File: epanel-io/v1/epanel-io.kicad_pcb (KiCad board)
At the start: 2 copper layers, 87 x 68 mm, 38 parts, among them J1 Conn_01x05_Male, J2 Screw_Terminal_01x03, J3 Screw_Terminal_01x03, Q1 IRF830, Q2 IRF830, Q3 IRF830, Q4 IRF830, U1 Pico, U2 4N35, U3 4N35, U4 H11AA1, U5 H11AA1, U6 H11AA1

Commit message: ok let's go!
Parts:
- removed JP1: Jumper_2_Bridged, Connector_PinHeader_2.54mm:PinHeader_1x02_P2.54mm_Vertical
- removed PS1: HLK-PM01, Converter_ACDC:Converter_ACDC_HiLink_HLK-PMxx
- added C10: 2.2uF/63V, Capacitor_SMD:C_1206_3216Metric, F.Cu at (434.5, 170.8)
- added C3: 2.2uF/63V, Capacitor_SMD:C_1206_3216Metric, F.Cu at (435.5, 59.6)
- added C4: 2.2uF/63V, Capacitor_SMD:C_1206_3216Metric, F.Cu at (356.4, 181.3)
- added C5: 2.2uF/63V, Capacitor_SMD:C_1206_3216Metric, F.Cu at (538.9, 59.6)
- added C6: 2.2uF/63V, Capacitor_SMD:C_1206_3216Metric, F.Cu at (472.8, 59.6)
- added C7: 2.2uF/63V, Capacitor_SMD:C_1206_3216Metric, F.Cu at (493.2, 115.2)
- added C8: 2.2uF/63V, Capacitor_SMD:C_1206_3216Metric, F.Cu at (509.1, 170.8)
- added C9: 2.2uF/63V, Capacitor_SMD:C_1206_3216Metric, F.Cu at (576.2, 59.6)
- added D10: 1N4007, Diode_SMD:D_SMA, F.Cu at (540.1, 55.6)
- added D11: 10V/0.4W, Diode_SMD:D_SOD-123, F.Cu at (490.5, 39.6)
- added D12: 1N4007, Diode_SMD:D_SMA, F.Cu at (474.0, 55.6)
- added D13: 10V/0.4W, Diode_SMD:D_SOD-123, F.Cu at (510.9, 95.2)
- added D14: 1N4007, Diode_SMD:D_SMA, F.Cu at (494.4, 111.3)
- added D15: 10V/0.4W, Diode_SMD:D_SOD-123, F.Cu at (526.8, 150.8)
- added D16: 1N4007, Diode_SMD:D_SMA, F.Cu at (510.3, 166.9)
- added D17: 10V/0.4W, Diode_SMD:D_SOD-123, F.Cu at (594.0, 39.6)
- added D18: 1N4007, Diode_SMD:D_SMA, F.Cu at (577.4, 55.6)
- added D19: 10V/0.4W, Diode_SMD:D_SOD-123, F.Cu at (452.2, 150.8)
- added D20: 1N4007, Diode_SMD:D_SMA, F.Cu at (435.7, 166.9)
- added D5: 10V/0.4W, Diode_SMD:D_SOD-123, F.Cu at (453.2, 39.6)
- added D6: 1N4007, Diode_SMD:D_SMA, F.Cu at (436.7, 55.6)
- added D7: 10V/0.4W, Diode_SMD:D_SOD-123, F.Cu at (374.1, 161.3)
- added D8: 1N4007, Diode_SMD:D_SMA, F.Cu at (357.6, 177.4)
- added D9: 10V/0.4W, Diode_SMD:D_SOD-123, F.Cu at (556.7, 39.6)
- added J4: Screw_Terminal_01x05, TerminalBlock:TerminalBlock_bornier-5_P5.08mm, F.Cu at (319.5, 86.8)
- added J5: Screw_Terminal_01x05, TerminalBlock:TerminalBlock_bornier-5_P5.08mm, F.Cu at (343.6, 42.2)
- added J6: Screw_Terminal_01x03, TerminalBlock:TerminalBlock_bornier-3_P5.08mm, F.Cu at (343.6, 51.3)
- added J7: Screw_Terminal_01x03, TerminalBlock:TerminalBlock_bornier-3_P5.08mm, F.Cu at (370.5, 42.2)
- added Q10: IRF830, Package_TO_SOT_SMD:TO-263-3_TabPin2, F.Cu at (544.9, 47.2)
- added Q11: IRF830, Package_TO_SOT_SMD:TO-263-3_TabPin2, F.Cu at (478.8, 34.8)
- added Q12: IRF830, Package_TO_SOT_SMD:TO-263-3_TabPin2, F.Cu at (478.8, 47.2)
- added Q13: IRF830, Package_TO_SOT_SMD:TO-263-3_TabPin2, F.Cu at (499.2, 90.5)
- added Q14: IRF830, Package_TO_SOT_SMD:TO-263-3_TabPin2, F.Cu at (499.2, 102.8)
- added Q15: IRF830, Package_TO_SOT_SMD:TO-263-3_TabPin2, F.Cu at (515.1, 146.1)
- added Q16: IRF830, Package_TO_SOT_SMD:TO-263-3_TabPin2, F.Cu at (515.1, 158.4)
- added Q17: IRF830, Package_TO_SOT_SMD:TO-263-3_TabPin2, F.Cu at (582.2, 34.8)
- added Q18: IRF830, Package_TO_SOT_SMD:TO-263-3_TabPin2, F.Cu at (582.2, 47.2)
- added Q19: IRF830, Package_TO_SOT_SMD:TO-263-3_TabPin2, F.Cu at (440.5, 146.1)
- added Q20: IRF830, Package_TO_SOT_SMD:TO-263-3_TabPin2, F.Cu at (440.5, 158.4)
- added Q5: IRF830, Package_TO_SOT_SMD:TO-263-3_TabPin2, F.Cu at (441.5, 34.8)
- added Q6: IRF830, Package_TO_SOT_SMD:TO-263-3_TabPin2, F.Cu at (441.5, 47.2)
- added Q7: IRF830, Package_TO_SOT_SMD:TO-263-3_TabPin2, F.Cu at (362.4, 156.6)
- added Q8: IRF830, Package_TO_SOT_SMD:TO-263-3_TabPin2, F.Cu at (362.4, 168.9)
- added Q9: IRF830, Package_TO_SOT_SMD:TO-263-3_TabPin2, F.Cu at (544.9, 34.8)
- added R18: 10KΩ, Resistor_SMD:R_0603_1608Metric, F.Cu at (404.8, 153.3)
- added R19: 33KΩ/0.5W, Resistor_SMD:R_0805_2012Metric, F.Cu at (418.2, 141.4)
- added R20: 33KΩ/0.5W, Resistor_SMD:R_0805_2012Metric, F.Cu at (405.0, 150.6)
- added R21: 330Ω, Resistor_SMD:R_0603_1608Metric, F.Cu at (434.6, 62.5)
- added R22: 22KΩ, Resistor_SMD:R_0603_1608Metric, F.Cu at (463.6, 32.9)
- added R23: 33KΩ/0.5W, Resistor_SMD:R_0805_2012Metric, F.Cu at (442.9, 54.8)
- added R24: 33KΩ/0.5W, Resistor_SMD:R_0805_2012Metric, F.Cu at (463.8, 30.1)
- added R25: 10KΩ, Resistor_SMD:R_0603_1608Metric, F.Cu at (463.5, 97.7)
- added R26: 33KΩ/0.5W, Resistor_SMD:R_0805_2012Metric, F.Cu at (476.8, 85.8)
- added R27: 33KΩ/0.5W, Resistor_SMD:R_0805_2012Metric, F.Cu at (463.7, 95.0)
- added R28: 330Ω, Resistor_SMD:R_0603_1608Metric, F.Cu at (355.6, 184.3)
- added R29: 22KΩ, Resistor_SMD:R_0603_1608Metric, F.Cu at (384.5, 154.6)
- added R30: 33KΩ/0.5W, Resistor_SMD:R_0805_2012Metric, F.Cu at (363.8, 176.6)
- added R31: 33KΩ/0.5W, Resistor_SMD:R_0805_2012Metric, F.Cu at (384.7, 151.9)
- added R32: 10KΩ, Resistor_SMD:R_0603_1608Metric, F.Cu at (318.3, 108.3)
- added R33: 33KΩ/0.5W, Resistor_SMD:R_0805_2012Metric, F.Cu at (331.6, 96.3)
- added R34: 33KΩ/0.5W, Resistor_SMD:R_0805_2012Metric, F.Cu at (318.5, 105.5)
- added R35: 330Ω, Resistor_SMD:R_0603_1608Metric, F.Cu at (538.1, 62.5)
- added R36: 22KΩ, Resistor_SMD:R_0603_1608Metric, F.Cu at (567.0, 32.9)
- added R37: 33KΩ/0.5W, Resistor_SMD:R_0805_2012Metric, F.Cu at (546.3, 54.8)
- added R38: 33KΩ/0.5W, Resistor_SMD:R_0805_2012Metric, F.Cu at (567.2, 30.1)
- added R39: 10KΩ, Resistor_SMD:R_0603_1608Metric, F.Cu at (509.2, 42.1)
- added R40: 33KΩ/0.5W, Resistor_SMD:R_0805_2012Metric, F.Cu at (522.6, 30.1)
- added R41: 33KΩ/0.5W, Resistor_SMD:R_0805_2012Metric, F.Cu at (509.4, 39.4)
- added R42: 330Ω, Resistor_SMD:R_0603_1608Metric, F.Cu at (471.9, 62.5)
- added R43: 22KΩ, Resistor_SMD:R_0603_1608Metric, F.Cu at (500.9, 32.9)
- added R44: 33KΩ/0.5W, Resistor_SMD:R_0805_2012Metric, F.Cu at (480.2, 54.8)
- added R45: 33KΩ/0.5W, Resistor_SMD:R_0805_2012Metric, F.Cu at (501.1, 30.1)
- added R46: 10KΩ, Resistor_SMD:R_0603_1608Metric, F.Cu at (405.8, 42.1)
- added R47: 33KΩ/0.5W, Resistor_SMD:R_0805_2012Metric, F.Cu at (419.1, 30.1)
- added R48: 33KΩ/0.5W, Resistor_SMD:R_0805_2012Metric, F.Cu at (406.0, 39.4)
- added R49: 330Ω, Resistor_SMD:R_0603_1608Metric, F.Cu at (492.3, 118.1)
- added R50: 22KΩ, Resistor_SMD:R_0603_1608Metric, F.Cu at (521.3, 88.5)
- added R51: 33KΩ/0.5W, Resistor_SMD:R_0805_2012Metric, F.Cu at (500.6, 110.5)
- added R52: 33KΩ/0.5W, Resistor_SMD:R_0805_2012Metric, F.Cu at (521.5, 85.8)
- added R53: 10KΩ, Resistor_SMD:R_0603_1608Metric, F.Cu at (405.8, 97.7)
- added R54: 33KΩ/0.5W, Resistor_SMD:R_0805_2012Metric, F.Cu at (419.1, 85.8)
- added R55: 33KΩ/0.5W, Resistor_SMD:R_0805_2012Metric, F.Cu at (406.0, 95.0)
- added R56: 330Ω, Resistor_SMD:R_0603_1608Metric, F.Cu at (508.3, 173.7)
- added R57: 22KΩ, Resistor_SMD:R_0603_1608Metric, F.Cu at (537.2, 144.1)
- added R58: 33KΩ/0.5W, Resistor_SMD:R_0805_2012Metric, F.Cu at (516.5, 166.1)
- added R59: 33KΩ/0.5W, Resistor_SMD:R_0805_2012Metric, F.Cu at (537.4, 141.4)
- added R60: 10KΩ, Resistor_SMD:R_0603_1608Metric, F.Cu at (434.6, 97.7)
- added R61: 33KΩ/0.5W, Resistor_SMD:R_0805_2012Metric, F.Cu at (448.0, 85.8)
- added R62: 33KΩ/0.5W, Resistor_SMD:R_0805_2012Metric, F.Cu at (434.8, 95.0)
- added R63: 330Ω, Resistor_SMD:R_0603_1608Metric, F.Cu at (575.4, 62.5)
- added R64: 22KΩ, Resistor_SMD:R_0603_1608Metric, F.Cu at (604.3, 32.9)
- added R65: 33KΩ/0.5W, Resistor_SMD:R_0805_2012Metric, F.Cu at (583.6, 54.8)
- added R66: 33KΩ/0.5W, Resistor_SMD:R_0805_2012Metric, F.Cu at (604.5, 30.1)
- added R67: 10KΩ, Resistor_SMD:R_0603_1608Metric, F.Cu at (529.6, 97.7)
- added R68: 33KΩ/0.5W, Resistor_SMD:R_0805_2012Metric, F.Cu at (543.0, 85.8)
- added R69: 33KΩ/0.5W, Resistor_SMD:R_0805_2012Metric, F.Cu at (529.8, 95.0)
- added R70: 330Ω, Resistor_SMD:R_0603_1608Metric, F.Cu at (433.7, 173.7)
- added R71: 22KΩ, Resistor_SMD:R_0603_1608Metric, F.Cu at (462.6, 144.1)
- added R72: 33KΩ/0.5W, Resistor_SMD:R_0805_2012Metric, F.Cu at (441.9, 166.1)
- added R73: 33KΩ/0.5W, Resistor_SMD:R_0805_2012Metric, F.Cu at (462.8, 141.4)
- added U10: 4N35, Package_DIP:SMDIP-6_W7.62mm, F.Cu at (376.9, 155.0)
- added U11: H11AA1, Package_DIP:SMDIP-6_W9.53mm, F.Cu at (322.9, 99.4)
- added U12: 4N35, Package_DIP:SMDIP-6_W7.62mm, F.Cu at (559.4, 33.3)
- added U13: H11AA1, Package_DIP:SMDIP-6_W9.53mm, F.Cu at (513.8, 33.3)
- added U14: 4N35, Package_DIP:SMDIP-6_W7.62mm, F.Cu at (493.3, 33.3)
- added U15: H11AA1, Package_DIP:SMDIP-6_W9.53mm, F.Cu at (410.4, 33.3)
- added U16: 4N35, Package_DIP:SMDIP-6_W7.62mm, F.Cu at (513.7, 88.9)
- added U17: H11AA1, Package_DIP:SMDIP-6_W9.53mm, F.Cu at (410.4, 88.9)
- added U18: 4N35, Package_DIP:SMDIP-6_W7.62mm, F.Cu at (529.6, 144.5)
- added U19: H11AA1, Package_DIP:SMDIP-6_W9.53mm, F.Cu at (439.2, 88.9)
- added U20: 4N35, Package_DIP:SMDIP-6_W7.62mm, F.Cu at (596.7, 33.3)
- added U21: H11AA1, Package_DIP:SMDIP-6_W9.53mm, F.Cu at (534.2, 88.9)
- added U22: 4N35, Package_DIP:SMDIP-6_W7.62mm, F.Cu at (455.0, 144.5)
- added U7: H11AA1, Package_DIP:SMDIP-6_W9.53mm, F.Cu at (409.4, 144.5)
- added U8: 4N35, Package_DIP:SMDIP-6_W7.62mm, F.Cu at (456.0, 33.3)
- added U9: H11AA1, Package_DIP:SMDIP-6_W9.53mm, F.Cu at (468.1, 88.9)
- D2: value 10V/0.4W -> 1N4007; footprint Diode_SMD:D_SOD-123 -> Diode_SMD:D_SMA
- D3: value 1N4007 -> 10V/0.4W; footprint Diode_SMD:D_SMA -> Diode_SMD:D_SOD-123
- J2, J3: value Screw_Terminal_01x03 -> Screw_Terminal_01x05; footprint TerminalBlock:TerminalBlock_bornier-3_P5.08mm -> TerminalBlock:TerminalBlock_bornier-5_P5.08mm
- R1: value 330Ω -> 10KΩ
- R11: value 33KΩ/0.5W -> 10KΩ; footprint Resistor_SMD:R_0805_2012Metric -> Resistor_SMD:R_0603_1608Metric
- R14: value 33KΩ/0.5W -> 330Ω; footprint Resistor_SMD:R_0805_2012Metric -> Resistor_SMD:R_0603_1608Metric
- R15, R8: value 33KΩ/0.5W -> 22KΩ; footprint Resistor_SMD:R_0805_2012Metric -> Resistor_SMD:R_0603_1608Metric
- R2: value 330Ω -> 33KΩ/0.5W; footprint Resistor_SMD:R_0603_1608Metric -> Resistor_SMD:R_0805_2012Metric
- R3, R5: value 10KΩ -> 33KΩ/0.5W; footprint Resistor_SMD:R_0603_1608Metric -> Resistor_SMD:R_0805_2012Metric
- R6: value 22KΩ -> 33KΩ/0.5W; footprint Resistor_SMD:R_0603_1608Metric -> Resistor_SMD:R_0805_2012Metric
- R7: value 22KΩ -> 330Ω
- U2, U3: value 4N35 -> H11AA1; footprint Package_DIP:SMDIP-6_W7.62mm -> Package_DIP:SMDIP-6_W9.53mm
- U4, U6: value H11AA1 -> 4N35; footprint Package_DIP:SMDIP-6_W9.53mm -> Package_DIP:SMDIP-6_W7.62mm
- moved R10 392.6 mm to (500.1, 141.4), turned to 0 degrees
- moved U4 380.6 mm to (492.3, 144.5)
- moved R8 347.9 mm to (499.9, 144.1), turned to 0 degrees
- moved D1 343.9 mm to (489.5, 150.8), turned to 0 degrees
- moved Q1 332.9 mm to (477.8, 146.1)
- moved Q2 332.2 mm to (477.8, 158.4)
- moved C1 328.8 mm to (471.8, 170.8), turned to 0 degrees
- moved R7 316.6 mm to (471.0, 173.7), turned to 0 degrees
- moved R9 315.1 mm to (479.2, 166.1), turned to 0 degrees
- moved D2 314.2 mm to (473.0, 166.9), turned to 0 degrees
- moved R12 278.7 mm to (389.3, 96.3), turned to 0 degrees
- moved U5 265.9 mm to (380.6, 99.4)
- moved R13 260.4 mm to (376.2, 105.5), turned to 0 degrees
- moved R11 258.2 mm to (376.0, 108.3), turned to 0 degrees
- moved R15 241.2 mm to (347.2, 154.6), turned to 0 degrees
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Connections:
- D2 pad 1: Net-(C2-Pad1) -> Net-(D2-Pad1)
- D2 pad 2: Net-(C2-Pad2) -> /Input 1/NEUT
- D3 pad 1: Net-(D3-Pad1) -> Net-(C2-Pad1)
- D3 pad 2: NEUT -> Net-(C2-Pad2)
- D4 pad 2: NEUT -> /Input 1/NEUT
- J2 pad 1: LINE -> /Input 1/NEUT
- J2 pad 2: Net-(J2-Pad2) -> /Input 1/INPUT
- J2 pad 3: Net-(J2-Pad3) -> /Input 2/INPUT
- J3 pad 1: NEUT -> /Output 1/LINE
- J3 pad 2: Net-(J3-Pad2) -> /Output 1/OUTPUT
- J3 pad 3: Net-(J3-Pad3) -> /Output 2/OUTPUT
- Q1 pad 2: LINE -> /Output 1/LINE
- Q2 pad 2: Net-(J2-Pad2) -> /Output 1/OUTPUT
- Q3 pad 2: LINE -> /Output 1/LINE
- Q4 pad 2: Net-(J2-Pad3) -> /Output 2/OUTPUT
- R1 pad 2: Net-(R1-Pad2) -> +3V3
- R10 pad 1: NEUT -> Net-(D2-Pad1)
- R11 pad 1: Net-(J3-Pad2) -> /Input 2/RPI
- R11 pad 2: Net-(R11-Pad2) -> +3V3
- R12 pad 1: NEUT -> /Input 1/NEUT
- R13 pad 1: Net-(J3-Pad3) -> /Input 2/INPUT
- R14 pad 1: NEUT -> Net-(R14-Pad1)
- R14 pad 2: Net-(R14-Pad2) -> /Output 2/RPI
- R15 pad 1: LINE -> Net-(Q3-Pad1)
- R15 pad 2: Net-(R15-Pad2) -> Net-(C2-Pad2)
- R16 pad 1: Net-(D3-Pad1) -> Net-(R16-Pad1)
- R16 pad 2: Net-(R16-Pad2) -> Net-(C2-Pad1)
- R17 pad 2: Net-(R17-Pad2) -> Net-(R16-Pad1)
- R2 pad 1: Net-(R2-Pad1) -> NEUT
- R3 pad 1: Net-(R3-Pad1) -> LINE
- R3 pad 2: +3V3 -> Net-(R3-Pad2)
- R4 pad 1: Net-(R4-Pad1) -> /Input 1/RPI
- R5 pad 1: Net-(R5-Pad1) -> /Input 1/NEUT
- R5 pad 2: +3V3 -> Net-(R5-Pad2)
- R6 pad 1: Net-(Q1-Pad1) -> /Input 1/INPUT
- R6 pad 2: Net-(C1-Pad2) -> Net-(R6-Pad2)
- R7 pad 1: Net-(Q3-Pad1) -> Net-(R7-Pad1)
- R7 pad 2: Net-(C2-Pad2) -> /Output 1/RPI
- R8 pad 1: Net-(R16-Pad2) -> Net-(Q1-Pad1)
- R8 pad 2: Net-(C1-Pad1) -> Net-(C1-Pad2)
- R9 pad 1: Net-(R17-Pad2) -> Net-(R10-Pad2)
- R9 pad 2: Net-(C2-Pad1) -> Net-(C1-Pad1)
- U1 pad 10: unconnected-(U1-Pad10) -> /Input 2/RPI
- U1 pad 11: unconnected-(U1-Pad11) -> /Input 3/RPI
- U1 pad 12: unconnected-(U1-Pad12) -> /Input 4/RPI
- U1 pad 14: unconnected-(U1-Pad14) -> /Output 1/RPI
- U1 pad 15: unconnected-(U1-Pad15) -> /Output 2/RPI
- U1 pad 16: unconnected-(U1-Pad16) -> /Output 3/RPI
- U1 pad 17: Net-(R5-Pad1) -> /Output 4/RPI
- U1 pad 19: Net-(R3-Pad1) -> /Input 5/RPI
- U1 pad 20: Net-(R1-Pad2) -> /Input 6/RPI
- U1 pad 21: Net-(R4-Pad1) -> /Input 7/RPI
- U1 pad 22: Net-(R2-Pad2) -> /Input 8/RPI
- U1 pad 24: unconnected-(U1-Pad24) -> /Output 5/RPI
- U1 pad 25: unconnected-(U1-Pad25) -> /Output 7/RPI
- U1 pad 26: unconnected-(U1-Pad26) -> /Output 6/RPI
- U1 pad 27: unconnected-(U1-Pad27) -> /Output 8/RPI
- U1 pad 29: unconnected-(U1-Pad29) -> /Input 9/RPI
- U1 pad 31: unconnected-(U1-Pad31) -> /Input 10/RPI
- U1 pad 32: unconnected-(U1-Pad32) -> /Output 9/RPI
- U1 pad 34: unconnected-(U1-Pad34) -> /Output 10/RPI
- U1 pad 39: Net-(JP1-Pad1) -> +5V
- U1 pad 4: unconnected-(U1-Pad4) -> Net-(R1-Pad1)
- U1 pad 9: unconnected-(U1-Pad9) -> /Input 1/RPI
- U2 pad 1: Net-(R1-Pad1) -> Net-(R2-Pad2)
- U2 pad 2: GND -> Net-(R3-Pad2)
- U2 pad 4: Net-(Q1-Pad1) -> GND
- U2 pad 5: Net-(C1-Pad1) -> Net-(R1-Pad1)
- U3 pad 1: Net-(R2-Pad1) -> Net-(R5-Pad2)
- U3 pad 2: GND -> Net-(R6-Pad2)
- U3 pad 4: Net-(Q3-Pad1) -> GND
- U3 pad 5: Net-(C2-Pad1) -> /Input 1/RPI
- U4 pad 1: Net-(R10-Pad2) -> Net-(R7-Pad1)
- U4 pad 2: Net-(R11-Pad2) -> GND
- U4 pad 4: GND -> Net-(Q1-Pad1)
- U4 pad 5: Net-(R3-Pad1) -> Net-(C1-Pad1)
- U5 pad 5: Net-(R4-Pad1) -> /Input 2/RPI
- U6 pad 1: Net-(R14-Pad2) -> Net-(R14-Pad1)
- U6 pad 2: Net-(R15-Pad2) -> GND
- U6 pad 4: GND -> Net-(Q3-Pad1)
- U6 pad 5: Net-(R5-Pad1) -> Net-(C2-Pad1)
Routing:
- net GND: track 166.4 -> 0.00 mm, vias 1 -> 0
- net NEUT: track 136.0 -> 0.00 mm, vias 5 -> 0
- net +5V: track 100.7 -> 0.00 mm, vias 2 -> 0
- net Net-(Q1-Pad1): track 87.5 -> 0.00 mm, vias 4 -> 0
- net Net-(R3-Pad1): track 77.3 -> 0.00 mm
- net Net-(R4-Pad1): track 74.4 -> 0.00 mm
- net LINE: track 68.3 -> 0.00 mm
- net Net-(Q3-Pad1): track 64.5 -> 0.00 mm, vias 4 -> 0
- net Net-(R5-Pad1): track 61.4 -> 0.00 mm
- net Net-(J1-Pad3): track 54.4 -> 0.00 mm
- net Net-(J1-Pad4): track 52.2 -> 0.00 mm
- net Net-(J1-Pad5): track 50.4 -> 0.00 mm
- net Net-(C1-Pad1): track 48.3 -> 0.00 mm, vias 2 -> 0
- net Net-(R15-Pad2): track 46.7 -> 0.00 mm
- net Net-(J2-Pad2): track 42.4 -> 0.00 mm
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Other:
- board text removed: "5V5"
- board text removed: "GND"
- board text removed: "I1"
- board text removed: "I2"
- board text removed: "INTR"
- board text removed: "L"
- board text removed: "N"
- board text removed: "O 1"
- board text removed: "O 2"
- board text removed: "SCL"
- board text removed: "SDA"

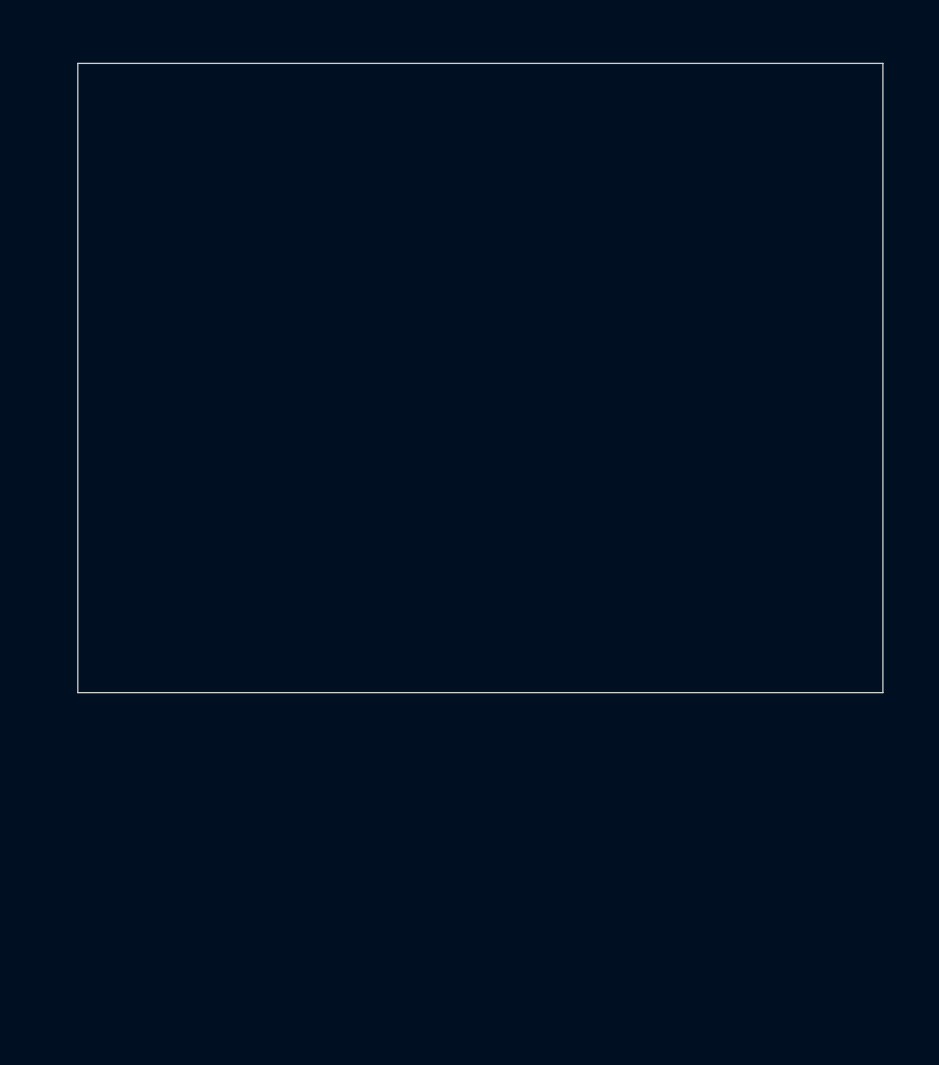
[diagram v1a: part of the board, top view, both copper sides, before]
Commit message: add dimensions
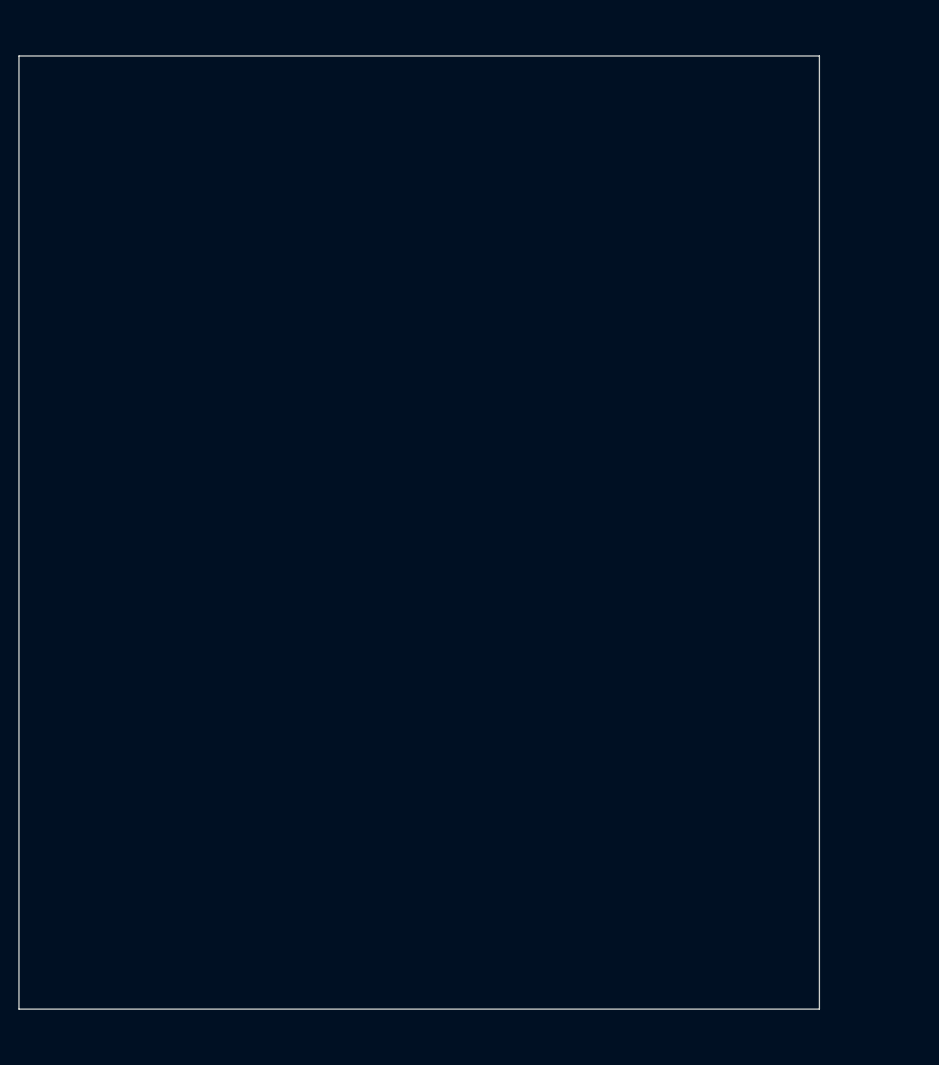
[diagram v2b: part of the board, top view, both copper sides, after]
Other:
- board size 87 x 68 mm -> 86.5 x 103 mm
- board text added: "CNMB/6- PCB A -> 86.5x103mm PCB B -> 57x102mm PCB C -> 42x102mm"
- board text removed: "Size: 87 x 68"
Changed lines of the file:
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@@
     )
   )
-  (gr_line locked (start 106.36 50.8) (end 193.36 50.8) (layer "Edge.Cuts") (width 0.1))
-  (gr_line locked (start 106.36 118.8) (end 106.36 50.8) (layer "Edge.Cuts") (width 0.1))
-  (gr_line locked (start 193.36 118.8) (end 193.36 50.8) (layer "Edge.Cuts") (width 0.1))
-  (gr_line locked (start 106.36 118.8) (end 193.36 118.8) (layer "Edge.Cuts") (width 0.1))
-  (gr_text "Size: 87 x 68" (at 198.12 172.72) (layer "Cmts.User")
-    (effects (font (size 3 3) (thickness 0.15)))
+  (gr_line locked (start 100 50) (end 186.5 50) (layer "Edge.Cuts") (width 0.1))
+  (gr_line locked (start 100 153) (end 100 50) (layer "Edge.Cuts") (width 0.1))
+  (gr_line locked (start 186.5 153) (end 186.5 50) (layer "Edge.Cuts") (width 0.1))
+  (gr_line locked (start 100 153) (end 186.5 153) (layer "Edge.Cuts") (width 0.1))
+  (gr_text "CNMB/6- \nPCB A -> 86.5x103mm\nPCB B -> 57x102mm\nPCB C -> 42x102mm" (at 178.435 173.99) (layer "Cmts.User")
+    (effects (font (size 2 2) (thickness 0.15)) (justify left))
   )
 )

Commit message: wip pcb
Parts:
- moved U4 418.5 mm to (83.8, 53.3)
- moved R7 413.6 mm to (74.3, 56.5)
- moved U8 374.7 mm to (83.8, 76.8)
- moved R21 359.9 mm to (75.1, 80.0)
- moved R10 356.2 mm to (152.4, 64.1), turned to 90 degrees
- moved D2 341.5 mm to (147.3, 64.1), turned to 180 degrees
- moved R9 339.9 mm to (154.9, 64.1), turned to -90 degrees
- moved Q1 338.1 mm to (151.8, 56.5), turned to 180 degrees
- moved D1 336.3 mm to (164.5, 64.8)
- moved R8 335.6 mm to (174.0, 64.1), turned to -90 degrees
- moved C1 330.5 mm to (158.8, 64.8)
- moved Q2 325.3 mm to (168.9, 56.5), turned to 180 degrees
- moved U10 299.5 mm to (84.5, 90.2)
- moved R22 297.2 mm to (170.1, 79.7)
- moved R24 297.2 mm to (170.3, 77.0)
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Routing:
- net /Output 1/LINE: track 0.00 -> 102.4 mm, vias 0 -> 2
- net /Output 2/OUTPUT: track 0.00 -> 63.0 mm, vias 0 -> 1
- net Net-(C1-Pad2): track 0.00 -> 51.8 mm, vias 0 -> 2
- net /Output 1/OUTPUT: track 0.00 -> 29.3 mm, vias 0 -> 1
- net Net-(Q1-Pad1): track 0.00 -> 23.2 mm
- net Net-(C2-Pad2): track 0.00 -> 22.3 mm, vias 0 -> 2
- net Net-(C1-Pad1): track 0.00 -> 9.40 mm
- net Net-(D2-Pad1): track 0.00 -> 3.46 mm
- net Net-(R10-Pad2): track 0.00 -> 2.54 mm

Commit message: wip pcb
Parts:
- moved C10 630.3 mm to (-195.5, 152.7)
- moved C5 630.3 mm to (-91.1, 41.5)
- moved C6 630.3 mm to (-157.2, 41.5)
- moved C7 630.3 mm to (-136.8, 97.1)
- moved C8 630.3 mm to (-120.9, 152.7)
- moved C9 630.3 mm to (-53.8, 41.5)
- moved D10 630.3 mm to (-89.9, 37.5)
- moved D11 630.3 mm to (-139.5, 21.5)
- moved D12 630.3 mm to (-156.0, 37.5)
- moved D13 630.3 mm to (-119.1, 77.1)
- moved D14 630.3 mm to (-135.6, 93.1)
- moved D15 630.3 mm to (-103.2, 132.7)
- moved D16 630.3 mm to (-119.7, 148.8)
- moved D17 630.3 mm to (-36.1, 21.5)
- moved D18 630.3 mm to (-52.6, 37.5)
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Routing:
- net /Input 1/NEUT: track 0.00 -> 51.8 mm, vias 0 -> 2
- net Net-(Q3-Pad1): track 0.00 -> 22.9 mm
- net Net-(C2-Pad1): track 0.00 -> 9.00 mm
- net Net-(C2-Pad2): track 22.3 -> 26.4 mm
- net Net-(D4-Pad1): track 0.00 -> 3.47 mm
- net Net-(C1-Pad2): track 51.8 -> 49.2 mm
- net Net-(R16-Pad1): track 0.00 -> 2.54 mm
- net /Output 1/LINE: track 102.4 -> 100.7 mm

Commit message: first 4 placement
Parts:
- moved Q5 16.9 mm to (151.8, 73.3)
- moved Q6 16.9 mm to (169.0, 73.3)
- moved Q7 16.9 mm to (117.6, 73.3)
- moved Q8 16.9 mm to (134.7, 73.3)
- moved R24 15.9 mm to (154.9, 81.3), turned to 90 degrees
- moved C3 13.1 mm to (166.8, 81.9)
- moved R31 11.1 mm to (121.3, 81.3), turned to 90 degrees
- moved C4 9.06 mm to (127.6, 81.9)
- moved D6 7.61 mm to (149.9, 81.3), turned to 180 degrees
- moved D7 7.45 mm to (133.3, 81.9)
- moved R23 7.41 mm to (157.5, 81.3), turned to -90 degrees
- moved R29 5.63 mm to (137.2, 81.3), turned to -90 degrees
- moved D8 5.10 mm to (116.2, 81.3), turned to 180 degrees
- moved R30 4.95 mm to (123.8, 81.3), turned to -90 degrees
- moved D5 4.07 mm to (161.3, 81.9)
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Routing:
- net /Output 4/OUTPUT: track 0.00 -> 66.2 mm, vias 0 -> 1
- net /Output 1/LINE: track 100.7 -> 161.2 mm
- net /Input 1/NEUT: track 51.8 -> 109.6 mm, vias 2 -> 4
- net Net-(C4-Pad2): track 0.00 -> 52.9 mm, vias 0 -> 3
- net Net-(C3-Pad2): track 0.00 -> 50.6 mm, vias 0 -> 2
- net /Output 3/OUTPUT: track 0.00 -> 33.8 mm, vias 0 -> 1
- net Net-(Q5-Pad1): track 0.00 -> 23.5 mm
- net Net-(Q7-Pad1): track 0.00 -> 23.5 mm
- net Net-(C2-Pad2): track 26.4 -> 43.8 mm, vias 2 -> 3
- net Net-(C4-Pad1): track 0.00 -> 9.00 mm
- net Net-(C3-Pad1): track 0.00 -> 8.73 mm
- net Net-(D8-Pad1): track 0.00 -> 3.51 mm
- net Net-(D6-Pad1): track 0.00 -> 3.51 mm
- net Net-(R30-Pad1): track 0.00 -> 2.54 mm
- net Net-(C1-Pad2): track 49.2 -> 46.6 mm
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
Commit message: wip
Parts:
- moved J5 479.9 mm to (182.2, 127.6), turned to -90 degrees
- moved J4 418.8 mm to (104.1, 127.6), turned to -90 degrees
- moved R42 365.6 mm to (197.8, 127.9)
- moved U14 361.5 mm to (205.1, 132.7)
- moved Q12 325.5 mm to (153.4, 143.6), turned to 90 degrees
- moved Q11 322.1 mm to (153.6, 120.7), turned to 90 degrees
- moved C6 314.0 mm to (149.5, 108.7)
- moved D12 314.0 mm to (150.7, 104.8)
- moved R44 314.0 mm to (156.9, 104.0)
- moved R45 302.3 mm to (157.8, 108.0)
- moved D11 301.6 mm to (151.8, 99.7)
- moved R43 298.0 mm to (153.7, 108.6)
- moved R35 295.1 mm to (197.7, 101.0)
- moved R49 294.7 mm to (148.0, 172.7)
- moved U16 292.9 mm to (157.5, 174.6)
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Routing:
- net /Output 5/LINE: track 0.00 -> 100.0 mm
- net /Output 5/OUTPUT: track 0.00 -> 39.9 mm, vias 0 -> 1
- net Net-(C5-Pad2): track 0.00 -> 38.3 mm, vias 0 -> 2
- net Net-(C7-Pad2): track 0.00 -> 26.6 mm
- net Net-(C6-Pad2): track 0.00 -> 26.5 mm
- net Net-(C8-Pad2): track 0.00 -> 26.4 mm
- net Net-(Q10-Pad1): track 0.00 -> 26.2 mm
- net Net-(Q11-Pad1): track 0.00 -> 26.2 mm
- net Net-(Q13-Pad1): track 0.00 -> 25.9 mm
- net Net-(Q15-Pad1): track 0.00 -> 25.8 mm
- net Net-(D10-Pad1): track 0.00 -> 19.2 mm, vias 0 -> 2
- net /Output 8/OUTPUT: track 0.00 -> 9.15 mm
- net /Output 7/OUTPUT: track 0.00 -> 9.15 mm
- net /Output 6/OUTPUT: track 0.00 -> 9.15 mm
- net Net-(C5-Pad1): track 0.00 -> 2.61 mm

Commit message: ?
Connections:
- R2 pad 1: NEUT -> /Input 10/NEUT
- R3 pad 1: LINE -> /Output 10/LINE

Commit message: wip remove components on power pcb
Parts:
- moved J7 445.4 mm to (182.2, 80.6), turned to -90 degrees
- moved J6 393.5 mm to (104.1, 81.3), turned to -90 degrees
- moved J1 381.8 mm to (102.9, 109.9)
- moved C5 31.6 mm to (176.5, 102.2)
- moved D9 29.0 mm to (175.9, 102.2)
- moved R36 28.8 mm to (174.6, 104.1)
- moved R37 21.8 mm to (179.1, 108.2)
- moved R38 18.2 mm to (175.9, 107.6)
- moved Q11 6.25 mm to (151.1, 126.5)
- moved Q13 6.25 mm to (136.9, 126.5)
- moved Q15 6.25 mm to (123.1, 126.5)
- moved Q9 6.25 mm to (164.9, 126.5)
- moved D10 5.71 mm to (167.0, 104.8)
- moved Q10 2.38 mm to (164.9, 143.4)
- moved Q12 2.38 mm to (151.1, 143.6)
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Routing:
- net /Output 8/OUTPUT: track 9.15 -> 87.8 mm, vias 0 -> 1
- net /Output 6/OUTPUT: track 9.15 -> 71.5 mm, vias 0 -> 1
- net /Output 7/OUTPUT: track 9.15 -> 56.3 mm, vias 0 -> 1
- net Net-(D10-Pad1): track 19.2 -> 0.00 mm, vias 2 -> 0
- net Net-(C5-Pad2): track 38.3 -> 21.8 mm, vias 2 -> 0
- net Net-(Q13-Pad1): track 25.9 -> 21.4 mm
- net Net-(Q15-Pad1): track 25.8 -> 21.4 mm
- net Net-(C8-Pad2): track 26.4 -> 22.1 mm
- net Net-(C6-Pad2): track 26.5 -> 22.1 mm
- net Net-(C7-Pad2): track 26.6 -> 22.2 mm
- net Net-(Q11-Pad1): track 26.2 -> 21.9 mm
- net Net-(Q10-Pad1): track 26.2 -> 22.1 mm
- net Net-(C5-Pad1): track 2.61 -> 0.00 mm
- net /Output 5/LINE: track 100.0 -> 97.6 mm
- net /Output 5/OUTPUT: track 39.9 -> 42.2 mm
